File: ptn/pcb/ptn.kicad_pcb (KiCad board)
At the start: 2 copper layers, 100 x 100 mm, 110 parts, among them IC1 ADP150AUJZ-3.3-R7, IC2 AZ1084CD-5.0TRG1, IC3 ADP150AUJZ-3.3-R7, IC4 GRF5509, J1 TB002-500-04BE, J10 142-0701-801, J2 NRF_CONN, J3 NRF_JUMPER_BANK, J4 ADC_IN_CONN, J5 POWER_OUT_CONN, J6 ADF_JUMPER_BANK, J7 MCP2551_JUMPER_BANK, J8 UART_CONN, J9 Conn_01x04, SW1 SW_Push, U1 MCP2551-I-SN, U2 NCP1117-3.3_SOT223, U3 ADF4351, U4 STM32F103C8T6, Y1 SIT5000AICGE-33E0-25.000000X, Y2 16MHz

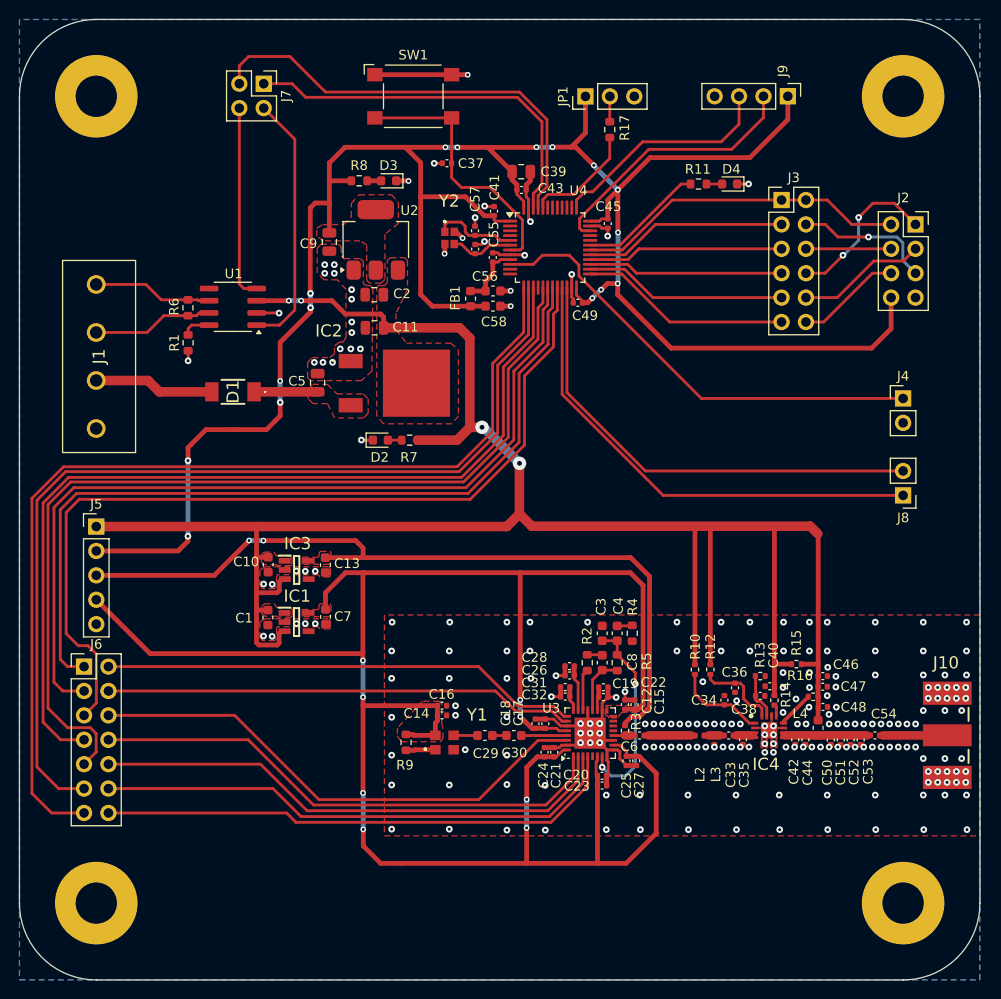
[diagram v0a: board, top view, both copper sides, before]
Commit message: Add silkscreen, add SW, fix NRF orientation, add stm32 BOOT1
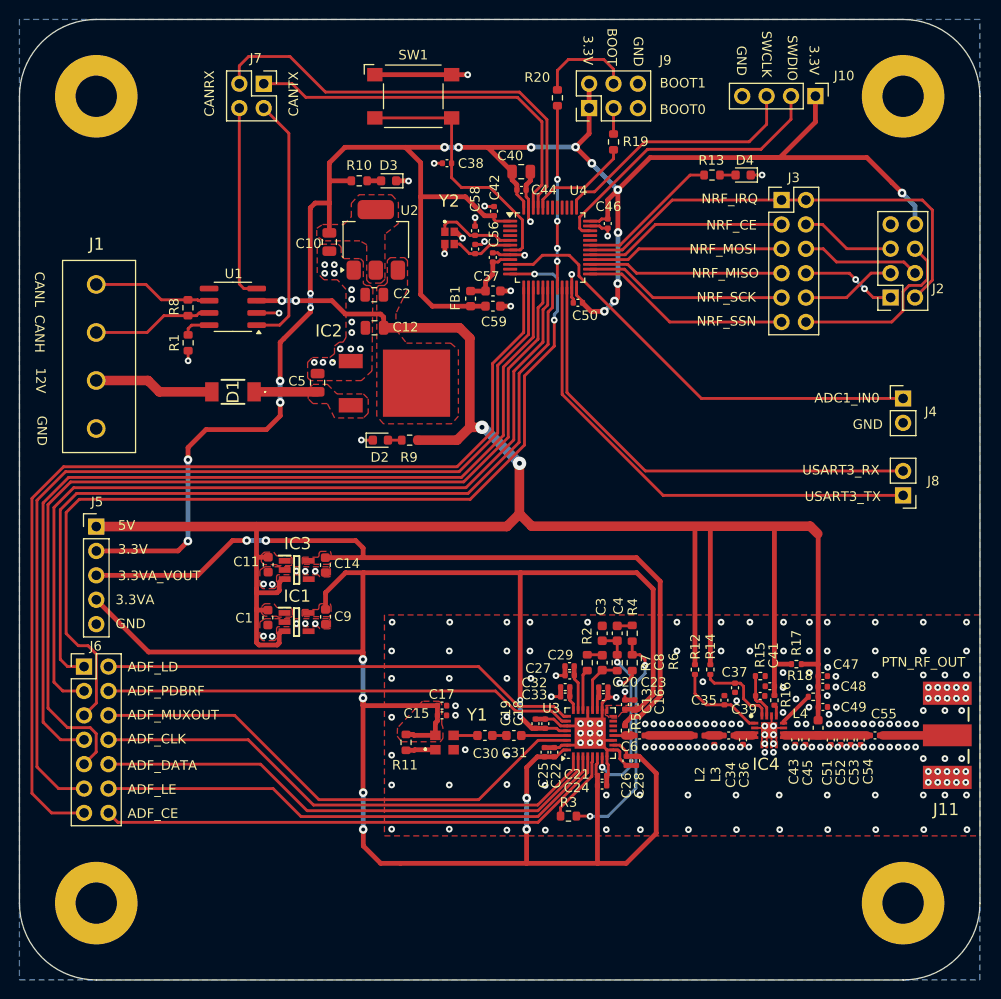
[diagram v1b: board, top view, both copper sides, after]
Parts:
- removed JP1: BOOT0_SEL, Connector_PinHeader_2.54mm:PinHeader_1x03_P2.54mm_Vertical
- removed the R17 at (133.5, 53.5)
- added J9: BOOT_SEL_JUMPER_BANK, Connector_PinHeader_2.54mm:PinHeader_2x03_P2.54mm_Vertical, F.Cu at (131.3, 51.2)
- added R19: 10k, Resistor_SMD:R_0603_1608Metric, F.Cu at (133.8, 54.8)
- added R20: 10k, Resistor_SMD:R_0603_1608Metric, F.Cu at (128.0, 50.2)
- added R3: ~, Resistor_SMD:R_0603_1608Metric, F.Cu at (129.2, 124.9)
- added R7: 0R, Resistor_SMD:R_0603_1608Metric, F.Cu at (135.8, 109.0)
- moved J2 8.04 mm to (162.7, 71.0), turned to 180 degrees
- moved J10 2.87 mm to (154.9, 50.0)
- moved D4 1.69 mm to (147.3, 58.2)
- moved R13 1.69 mm to (144.1, 58.2)
- renumbered C9 to C10, C10 to C11, C11 to C12, C12 to C13, C13 to C14, C14 to C15, C15 to C16, C16 to C17, C17 to C18, C18 to C19, C19 to C20, C20 to C21, C21 to C22, C22 to C23, C23 to C24, C24 to C25, C25 to C26, C26 to C27, C27 to C28, C28 to C29, C29 to C30, C30 to C31, C31 to C32, C32 to C33, C33 to C34, C34 to C35, C35 to C36, C36 to C37, C37 to C38, C38 to C39, C39 to C40, C40 to C41, C41 to C42, C42 to C43, C43 to C44, C44 to C45, C45 to C46, C46 to C47, C47 to C48, C48 to C49, C49 to C50, C50 to C51, C51 to C52, C52 to C53, C53 to C54, C54 to C55, C55 to C56, C56 to C57, C57 to C58, C58 to C59, C59 to C60, C7 to C9, J9 to J10, J10 to J11, R8 to R10, R9 to R11, R10 to R12, R11 to R13, R12 to R14, R13 to R15, R14 to R16, R15 to R17, R16 to R18, R3 to R5, R5 to R6, R6 to R8, R7 to R9
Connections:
- R4 pad 2: GND -> Net-(R3-Pad2)
- U3 pad 5: unconnected-(U3-SW-Pad5) -> ADF4351_SW
- U4 pad 12: unconnected-(U4-PA2-Pad12) -> STM32_ADF_MUXOUT
- U4 pad 20: STM32_ADF_MUXOUT -> STM32_BOOT1
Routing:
- net Net-(R3-Pad2): track 0.00 -> 24.1 mm, vias 0 -> 2
- net STM32_BOOT1: track 0.00 -> 18.9 mm, vias 0 -> 4
- net NRF24L01P_IRQ: track 34.5 -> 48.1 mm
- net Net-(J9-Pin_5): track 0.00 -> 10.3 mm
- net +3.3V: track 226.3 -> 217.4 mm, vias 16 -> 17
- net NRF24L01P_SSN: track 11.0 -> 19.4 mm
- net ADF4351_SW: track 0.00 -> 7.62 mm
- net NRF24L01P_MISO: track 16.7 -> 9.89 mm
- net STM32_ADF_MUXOUT: track 92.0 -> 98.0 mm, vias 0 -> 2
- net NRF24L01P_CE: track 14.6 -> 9.86 mm, vias 1 -> 0
- net NRF24L01P_SCK: track 13.5 -> 9.87 mm
- net NRF24L01P_MOSI: track 8.87 -> 12.4 mm
- net SWDIO: track 27.9 -> 31.0 mm
- net SWCLK: track 23.9 -> 26.8 mm
- net +3.3VA: track 214.8 -> 217.6 mm
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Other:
- board text added: "12V"
- board text added: "3.3V"
- board text added: "3.3VA"
- board text added: "3.3VA_VOUT"
- board text added: "5V"
- board text added: "ADC1_IN0"
- board text added: "ADF_CE"
- board text added: "ADF_CLK"
- board text added: "ADF_DATA"
- board text added: "ADF_LD"
- board text added: "ADF_LE"
- board text added: "ADF_MUXOUT"
- board text added: "ADF_PDBRF"
- board text added: "BOOT"
- board text added: "BOOT0"
- board text added: "BOOT1"
- board text added: "CANH"
- board text added: "CANL"
- board text added: "CANRX"
- board text added: "CANTX"
- board text added: "GND"
- board text added: "NRF_CE"
- board text added: "NRF_IRQ"
- board text added: "NRF_MISO"
- board text added: "NRF_MOSI"
- board text added: "NRF_SCK"
- board text added: "NRF_SSN"
- board text added: "PTN_RF_OUT"
- board text added: "SWCLK"
- board text added: "SWDIO"
- board text added: "USART3_RX"
- board text added: "USART3_TX"

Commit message: manufacturing ptn
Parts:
- added C13: 100p, Capacitor_SMD:C_0402_1005Metric, F.Cu at (135.0, 114.9)
- added C16: 120p, Capacitor_SMD:C_0402_1005Metric, F.Cu at (139.9, 109.8)
- added C20: 0.1u, Capacitor_SMD:C_0402_1005Metric, F.Cu at (139.9, 110.8)
- added C23: 120p, Capacitor_SMD:C_0402_1005Metric, F.Cu at (139.9, 111.8)
- added G***: LOGO, LOGO, F.Cu at (90.7, 134.0)
- added G***: LOGO, LOGO, B.Cu at (153.1, 134.0)
- added L2: 1.9n, Inductor_SMD:L_0402_1005Metric, F.Cu at (140.9, 116.5)
- added R10: 50R, Resistor_SMD:R_0402_1005Metric, F.Cu at (136.0, 114.9)
- added R11: 50R, Resistor_SMD:R_0402_1005Metric, F.Cu at (137.1, 112.9)
- added R15: 10k, Resistor_SMD:R_0603_1608Metric, F.Cu at (96.0, 113.2)
- added R16: 10k, Resistor_SMD:R_0603_1608Metric, F.Cu at (96.0, 126.9)
- added R17: 10k, Resistor_SMD:R_0603_1608Metric, F.Cu at (96.0, 118.3)
- added R18: 10k, Resistor_SMD:R_0603_1608Metric, F.Cu at (96.0, 120.8)
- added R19: 10k, Resistor_SMD:R_0603_1608Metric, F.Cu at (96.0, 123.3)
- moved C4 2.40 mm to (139.0, 116.5)
- moved R2 1.90 mm to (136.9, 116.0)
- moved C15 0.59 mm to (135.0, 112.7)
- moved C19 0.59 mm to (136.0, 112.7)
- renumbered C13 to C15, C14 to C17, C15 to C18, C16 to C19, C17 to C21, C18 to C22, C19 to C24, C20 to C25, C21 to C26, C22 to C27, C23 to C28, C24 to C29, C25 to C30, C26 to C31, C27 to C32, C28 to C33, C29 to C34, C30 to C35, C31 to C36, C32 to C37, C33 to C38, C34 to C39, C6 to C4, C35 to C40, C36 to C41, C37 to C42, C39 to C43, C41 to C44, C43 to C45, C45 to C46, C51 to C50, C52 to C51, C53 to C52, C54 to C53, C38 to C54, C40 to C56, C42 to C57, C44 to C58, C46 to C59, C4 to C6, C50 to C60, C56 to C61, C57 to C62, C58 to C63, C59 to C64, C60 to C65, C5 to C7, J9 to J10, J10 to J11, J11 to J9, L2 to L4, L3 to L5, L4 to L6, R9 to R12, R10 to R13, R11 to R14, R5 to R2, R12 to R20, R14 to R21, R15 to R22, R16 to R23, R17 to R24, R18 to R25, R13 to R26, R19 to R27, R20 to R28, R2 to R3, R3 to R4, R4 to R5, R8 to R9
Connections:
- C4 pad 2: GRF5509_RFIN -> Net-(C4-Pad2)
- U3 pad 13: unconnected-(U3-RF_OUT_A--Pad13) -> ADF4351_RFOUTA-
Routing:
- net +3.3VA: track 217.6 -> 241.5 mm
- net GRF5509_RFIN: track 4.44 -> 0.19 mm
- net GND: track 95.0 -> 99.1 mm, vias 228 -> 233
- net ADF4351_PDBRF: track 49.1 -> 52.1 mm
- net ADF4351_MOSI: track 54.1 -> 57.1 mm
- net ADF4351_SCK: track 54.1 -> 57.0 mm
- net Net-(C13-Pad2): track 0.00 -> 2.80 mm
- net ADF4351_SSN: track 54.1 -> 56.9 mm
- net ADF4351_RFOUTA-: track 0.00 -> 2.52 mm
- net ADF4351_CE: track 54.2 -> 56.4 mm
- net +3.3VA_VOUT: track 83.5 -> 85.6 mm
- net ADF4351_RFOUTA+: track 1.87 -> 3.40 mm
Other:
- board text added: "Power Transmitter Node"
- board text added: "Power Transmitter Node Ardavan Pourkeramati 2024-07"
